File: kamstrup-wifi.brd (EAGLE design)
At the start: 36 x 89.3 mm, 21 parts, among them T1 BT137, T2 BT137, U1 ESP8266-07

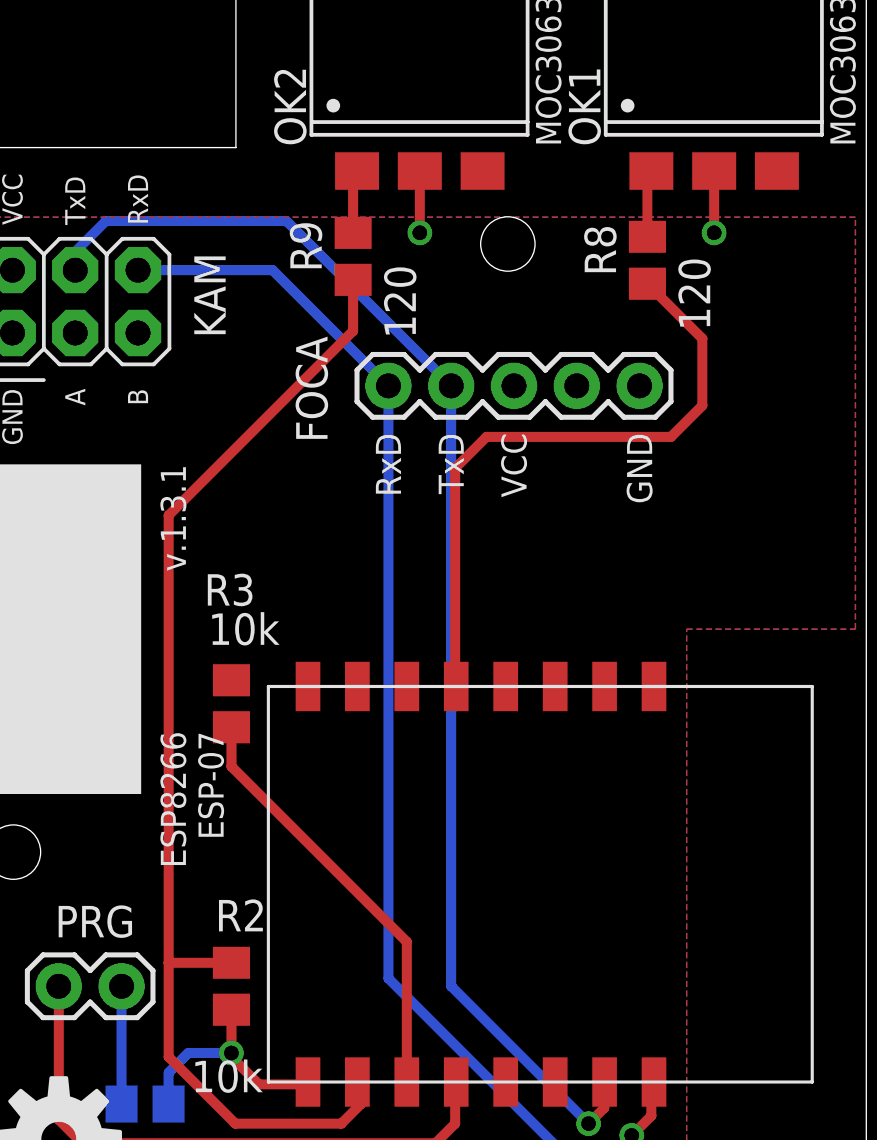
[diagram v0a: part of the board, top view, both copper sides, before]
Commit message: programmer connector moved
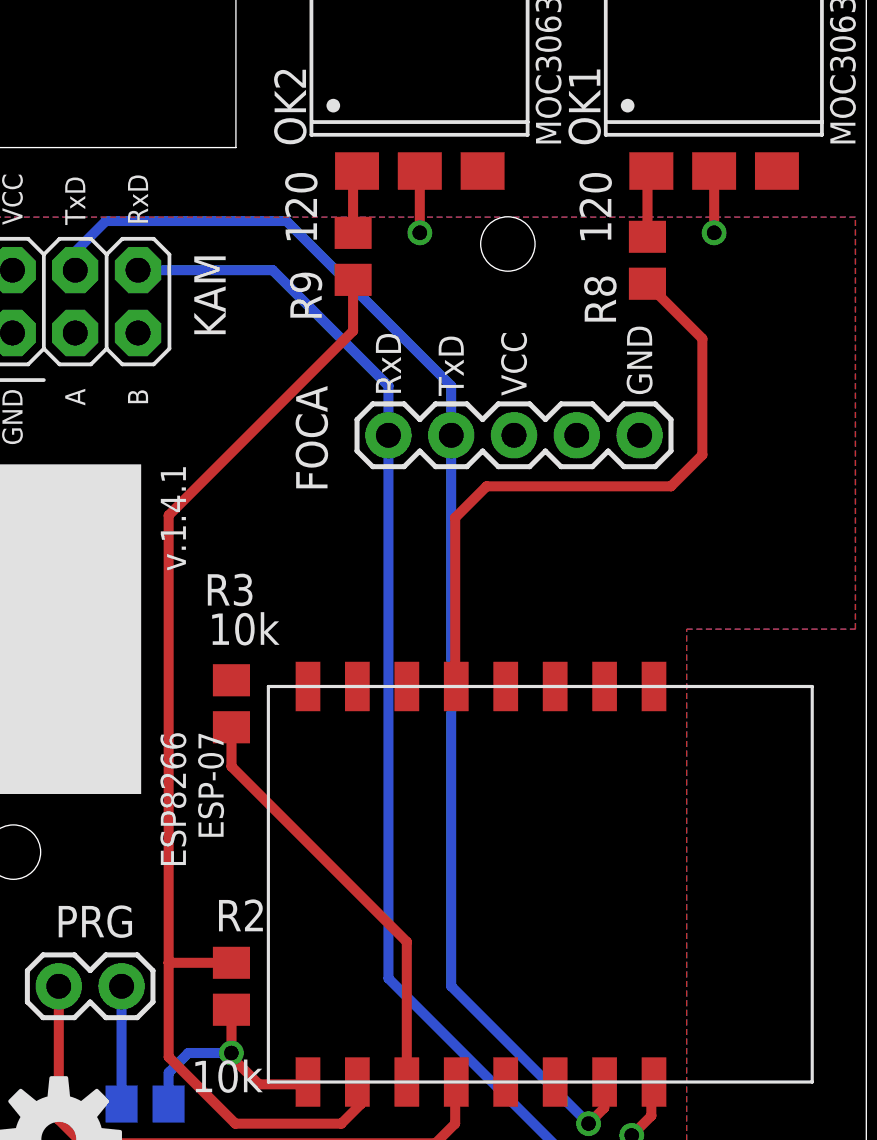
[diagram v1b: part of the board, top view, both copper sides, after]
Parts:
- moved FOCA 2.00 mm to (16.7, 30.9)
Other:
- board text added: "v.1.4.1"
- board text removed: "v.1.3.1"
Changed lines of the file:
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@@
 <?xml version="1.0" encoding="utf-8"?>
 <!DOCTYPE eagle SYSTEM "eagle.dtd">
-<eagle version="8.4.0">
+<eagle version="8.7.1">
 <drawing>
 <settings>
-<setting alwaysvectorfont="yes"/>
+<setting alwaysvectorfont="no"/>
 <setting keepoldvectorfont="yes"/>
 <setting verticaltext="up"/>
@@
 <hole x="1.5" y="14" drill="2.2"/>
 <hole x="21.5" y="38.6" drill="2.2"/>
-<text x="21.74875" y="30.95625" size="1.016" layer="25" rot="R90" align="center-right">VCC</text>
-<text x="19.20875" y="30.95625" size="1.016" layer="25" rot="R90" align="center-right">TxD</text>
-<text x="16.66875" y="30.95625" size="1.016" layer="25" rot="R90" align="center-right">RxD</text>
+<text x="21.74875" y="32.45625" size="1.016" layer="25" rot="R90" align="center-left">VCC</text>
+<text x="19.20875" y="32.45625" size="1.016" layer="25" rot="R90" align="center-left">TxD</text>
+<text x="16.66875" y="32.45625" size="1.016" layer="25" rot="R90" align="center-left">RxD</text>
 <text x="7.46125" y="18.89125" size="1.016" layer="25" ratio="10" rot="R270">ESP8266
 ESP-07</text>
-<text x="7.46125" y="29.68625" size="1.016" layer="25" ratio="15" rot="R270">v.1.3.1</text>
-<text x="26.82875" y="30.95625" size="1.016" layer="25" rot="R90" align="center-right">GND</text>
+<text x="7.46125" y="29.68625" size="1.016" layer="25" ratio="15" rot="R270">v.1.4.1</text>
+<text x="26.82875" y="32.45625" size="1.016" layer="25" rot="R90" align="center-left">GND</text>
 <text x="20.7725" y="75.615" size="1.27" layer="25" ratio="20" rot="R90" align="center">AC IN
 N   L</text>
@@
 <param name="dpMaxLengthDifference" value="10mm"/>
 <param name="dpGapFactor" value="2.5"/>
+<param name="checkAngle" value="0"/>
 <param name="checkFont" value="1"/>
 <param name="checkRestrict" value="1"/>
 <param name="checkStop" value="0"/>
+<param name="checkValues" value="0"/>
 <param name="useDiameter" value="13"/>
 <param name="maxErrors" value="50"/>
@@
 <attribute name="VALUE" x="0.19" y="31.825" size="1.27" layer="27"/>
 </element>
-<element name="FOCA" library="SparkFun-Connectors" package="1X05" value="" x="16.66875" y="32.86125" smashed="yes">
-<attribute name="NAME" x="14.20495" y="30.56255" size="1.27" layer="25" ratio="10" rot="R90"/>
-<attribute name="VALUE" x="15.39875" y="29.68625" size="1.27" layer="27"/>
+<element name="FOCA" library="SparkFun-Connectors" package="1X05" value="" x="16.66875" y="30.86125" smashed="yes">
+<attribute name="NAME" x="14.20495" y="28.56255" size="1.27" layer="25" ratio="10" rot="R90"/>
+<attribute name="VALUE" x="15.39875" y="27.68625" size="1.27" layer="27"/>
 </element>
 <element name="PRG" library="SparkFun-Connectors" package="1X02" value="M02PTH" x="5.87375" y="8.5725" smashed="yes" rot="R180">
@@
 </element>
 <element name="R9" library="rcl" package="R0805" value="120" x="15.24" y="38.1" smashed="yes" rot="R90">
-<attribute name="NAME" x="13.97" y="37.465" size="1.27" layer="25" rot="R90"/>
-<attribute name="VALUE" x="17.78" y="34.76625" size="1.27" layer="25" rot="R90"/>
+<attribute name="NAME" x="13.97" y="35.465" size="1.27" layer="25" rot="R90"/>
+<attribute name="VALUE" x="13.78" y="38.58375" size="1.27" layer="25" rot="R90"/>
 </element>
 <element name="R6" library="rcl" package="R0805" value="330" x="16.8275" y="67.945" smashed="yes" rot="MR180">
@@
 </element>
 <element name="R8" library="rcl" package="R0805" value="120" x="27.14625" y="37.94125" smashed="yes" rot="R90">
-<attribute name="NAME" x="25.87625" y="37.30625" size="1.27" layer="25" rot="R90"/>
-<attribute name="VALUE" x="29.68625" y="35.08375" size="1.27" layer="25" rot="R90"/>
+<attribute name="NAME" x="25.87625" y="35.30625" size="1.27" layer="25" rot="R90"/>
+<attribute name="VALUE" x="25.68625" y="38.58375" size="1.27" layer="25" rot="R90"/>
 </element>
 <element name="R4" library="rcl" package="R0805" value="330" x="27.78125" y="67.945" smashed="yes" rot="MR180">
@@
 <wire x1="25.7175" y1="1.74625" x2="23.8125" y2="1.74625" width="0.4064" layer="16"/>
 <wire x1="23.8125" y1="1.74625" x2="16.66875" y2="8.89" width="0.4064" layer="16"/>
-<wire x1="16.66875" y1="8.89" x2="16.66875" y2="32.86125" width="0.4064" layer="16"/>
+<wire x1="16.66875" y1="8.89" x2="16.66875" y2="30.86125" width="0.4064" layer="16"/>
 <wire x1="6.54" y1="37.54" x2="11.99" y2="37.54" width="0.4064" layer="16"/>
 <wire x1="11.99" y1="37.54" x2="16.66875" y2="32.86125" width="0.4064" layer="16"/>
+<wire x1="16.66875" y1="32.86125" x2="16.66875" y2="30.86125" width="0.4064" layer="16"/>
 </signal>
 <signal name="N$2">
@@
 <wire x1="25.4" y1="4.6875" x2="25.4" y2="3.65125" width="0.4064" layer="1"/>
 <wire x1="25.4" y1="3.65125" x2="24.765" y2="3.01625" width="0.4064" layer="1"/>
-<wire x1="19.20875" y1="32.86125" x2="19.20875" y2="8.5725" width="0.4064" layer="16"/>
+<wire x1="19.20875" y1="30.86125" x2="19.20875" y2="8.5725" width="0.4064" layer="16"/>
 <wire x1="19.20875" y1="8.5725" x2="24.765" y2="3.01625" width="0.4064" layer="16"/>
 <wire x1="5.23875" y1="39.52875" x2="12.54125" y2="39.52875" width="0.4064" layer="16"/>
 <wire x1="12.54125" y1="39.52875" x2="19.20875" y2="32.86125" width="0.4064" layer="16"/>
+<wire x1="19.20875" y1="32.86125" x2="19.20875" y2="30.86125" width="0.4064" layer="16"/>
 </signal>
 <signal name="N$4">
@@
 <wire x1="19.3675" y1="20.745" x2="19.4125" y2="20.7" width="0.4064" layer="1"/>
 <contactref element="R8" pad="1"/>
-<wire x1="19.3675" y1="20.745" x2="19.3675" y2="29.5275" width="0.4064" layer="1"/>
-<wire x1="19.3675" y1="29.5275" x2="20.6375" y2="30.7975" width="0.4064" layer="1"/>
-<wire x1="20.6375" y1="30.7975" x2="28.09875" y2="30.7975" width="0.4064" layer="1"/>
-<wire x1="28.09875" y1="30.7975" x2="29.36875" y2="32.0675" width="0.4064" layer="1"/>
-<wire x1="29.36875" y1="32.0675" x2="29.36875" y2="34.76875" width="0.4064" layer="1"/>
+<wire x1="19.3675" y1="20.745" x2="19.3675" y2="27.5275" width="0.4064" layer="1"/>
+<wire x1="19.3675" y1="27.5275" x2="20.6375" y2="28.7975" width="0.4064" layer="1"/>
+<wire x1="20.6375" y1="28.7975" x2="28.09875" y2="28.7975" width="0.4064" layer="1"/>
+<wire x1="28.09875" y1="28.7975" x2="29.36875" y2="30.0675" width="0.4064" layer="1"/>
+<wire x1="29.36875" y1="30.0675" x2="29.36875" y2="34.76875" width="0.4064" layer="1"/>
 <wire x1="29.36875" y1="34.76875" x2="27.14625" y2="36.99125" width="0.4064" layer="1"/>
 </signal>

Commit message: Sdcard
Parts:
- added U$1: MICROSD_SPI_MODE, con-molex-microsd:MICRO_SD_CONNECTOR
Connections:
- new net N$10: U$1.7, U1.GPIO12
- new net N$17: U$1.3, U1.GPIO13
- new net N$19: U$1.5, U1.GPIO14
- new net N$20: R2.2, U$1.2, U1.GPIO15
- net 3.3V: now also U$1.4
- net GND: now also U$1.6
- net N$11: now also U1.GPIO4; no longer U1.GPIO14
- net N$16: now also U1.GPIO5; no longer R2.2, U1.GPIO15
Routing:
- net N$1: track 51.7 -> 16.6 mm
- net N$2: track 53.3 -> 23.2 mm
- net N$16: track 47.3 -> 44.5 mm
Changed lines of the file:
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@@
 <?xml version="1.0" encoding="utf-8"?>
 <!DOCTYPE eagle SYSTEM "eagle.dtd">
-<eagle version="8.7.1">
+<eagle version="9.0.1">
 <drawing>
 <settings>
@@
 <text x="20.7725" y="75.615" size="1.27" layer="25" ratio="20" rot="R90" align="center">AC IN
 N   L</text>
-<text x="27.6225" y="13.0175" size="1.016" layer="26" font="fixed" rot="MR0">Part            RS#
+<text x="15.4825" y="32.6225" size="1.016" layer="26" font="fixed" rot="MR270">Part            RS#
 JP1, JP2, JP3   821-8701
 KAM             702-2937
@@
 T1, T2          792-0709
 </text>
-<wire x1="28.41625" y1="26.845" x2="14.2875" y2="26.845" width="0.1524" layer="26"/>
-<wire x1="14.2875" y1="26.845" x2="5.08" y2="26.845" width="0.1524" layer="26"/>
-<wire x1="5.08" y1="26.845" x2="5.08" y2="13.81125" width="0.1524" layer="26"/>
-<wire x1="5.08" y1="13.81125" x2="14.2875" y2="13.81125" width="0.1524" layer="26"/>
-<wire x1="14.2875" y1="13.81125" x2="28.41625" y2="13.81125" width="0.1524" layer="26"/>
-<wire x1="28.41625" y1="13.81125" x2="28.41625" y2="26.845" width="0.1524" layer="26"/>
-<wire x1="14.2875" y1="26.845" x2="14.2875" y2="13.81125" width="0.1524" layer="26"/>
+<wire x1="1.655" y1="33.41625" x2="1.655" y2="19.2875" width="0.1524" layer="26"/>
+<wire x1="1.655" y1="19.2875" x2="1.655" y2="10.08" width="0.1524" layer="26"/>
+<wire x1="1.655" y1="10.08" x2="14.68875" y2="10.08" width="0.1524" layer="26"/>
+<wire x1="14.68875" y1="10.08" x2="14.68875" y2="19.2875" width="0.1524" layer="26"/>
+<wire x1="14.68875" y1="19.2875" x2="14.68875" y2="33.41625" width="0.1524" layer="26"/>
+<wire x1="14.68875" y1="33.41625" x2="1.655" y2="33.41625" width="0.1524" layer="26"/>
+<wire x1="1.655" y1="19.2875" x2="14.68875" y2="19.2875" width="0.1524" layer="26"/>
 <wire x1="12.99375" y1="80.06" x2="16.9625" y2="80.06" width="0.254" layer="25"/>
 <wire x1="16.9625" y1="80.06" x2="16.9625" y2="70.2175" width="0.254" layer="25"/>
@@
 <attribute name="VALUE" x="9.36625" y="22.38375" size="1.27" layer="25"/>
 </element>
+<element name="U$1" library="con-molex-microsd" package="MICRO_SD_CONNECTOR" value="MICROSD_SPI_MODE" x="26.5" y="13.5" rot="MR270"/>
 </elements>
 <signals>
@@
 <contactref element="R2" pad="1"/>
 <wire x1="10.31875" y1="7.6225" x2="10.31875" y2="5.87375" width="0.4064" layer="1"/>
+<contactref element="U$1" pad="6"/>
+<wire x1="13.4125" y1="4.7" x2="18.3" y2="10.03" width="0" layer="19" extent="1-16"/>
 </signal>
 <signal name="3.3V">
@@
 <contactref element="U1" pad="VCC"/>
 <contactref element="R3" pad="1"/>
+<contactref element="U$1" pad="4"/>
+<wire x1="13.4125" y1="20.7" x2="18.3" y2="12.23" width="0" layer="19" extent="1-16"/>
 </signal>
 <signal name="N$1">
@@
 <wire x1="27.305" y1="3.33375" x2="27.305" y2="4.5925" width="0.4064" layer="1"/>
 <wire x1="27.305" y1="4.5925" x2="27.4125" y2="4.7" width="0.4064" layer="1"/>
-<wire x1="26.51125" y1="2.54" x2="25.7175" y2="1.74625" width="0.4064" layer="16"/>
-<wire x1="25.7175" y1="1.74625" x2="23.8125" y2="1.74625" width="0.4064" layer="16"/>
-<wire x1="23.8125" y1="1.74625" x2="16.66875" y2="8.89" width="0.4064" layer="16"/>
-<wire x1="16.66875" y1="8.89" x2="16.66875" y2="30.86125" width="0.4064" layer="16"/>
 <wire x1="6.54" y1="37.54" x2="11.99" y2="37.54" width="0.4064" layer="16"/>
 <wire x1="11.99" y1="37.54" x2="16.66875" y2="32.86125" width="0.4064" layer="16"/>
 <wire x1="16.66875" y1="32.86125" x2="16.66875" y2="30.86125" width="0.4064" layer="16"/>
+<wire x1="27.4125" y1="4.7" x2="16.66875" y2="30.86125" width="0" layer="19" extent="1-1"/>
 </signal>
 <signal name="N$2">
@@
 <wire x1="25.4" y1="4.6875" x2="25.4" y2="3.65125" width="0.4064" layer="1"/>
 <wire x1="25.4" y1="3.65125" x2="24.765" y2="3.01625" width="0.4064" layer="1"/>
-<wire x1="19.20875" y1="30.86125" x2="19.20875" y2="8.5725" width="0.4064" layer="16"/>
-<wire x1="19.20875" y1="8.5725" x2="24.765" y2="3.01625" width="0.4064" layer="16"/>
 <wire x1="5.23875" y1="39.52875" x2="12.54125" y2="39.52875" width="0.4064" layer="16"/>
 <wire x1="12.54125" y1="39.52875" x2="19.20875" y2="32.86125" width="0.4064" layer="16"/>
 <wire x1="19.20875" y1="32.86125" x2="19.20875" y2="30.86125" width="0.4064" layer="16"/>
+<wire x1="19.20875" y1="30.86125" x2="25.4125" y2="4.7" width="0" layer="19" extent="1-1"/>
 </signal>
 <signal name="N$4">
@@
 </signal>
 <signal name="N$11">
-<contactref element="U1" pad="GPIO14"/>
-<wire x1="19.3675" y1="20.745" x2="19.4125" y2="20.7" width="0.4064" layer="1"/>
 <contactref element="R8" pad="1"/>
 <wire x1="19.3675" y1="20.745" x2="19.3675" y2="27.5275" width="0.4064" layer="1"/>
@@
 <wire x1="29.36875" y1="30.0675" x2="29.36875" y2="34.76875" width="0.4064" layer="1"/>
 <wire x1="29.36875" y1="34.76875" x2="27.14625" y2="36.99125" width="0.4064" layer="1"/>
+<contactref element="U1" pad="GPIO4"/>
+<wire x1="23.4125" y1="4.7" x2="19.3675" y2="20.745" width="0" layer="19" extent="1-1"/>
 </signal>
 <signal name="N$16">
-<contactref element="U1" pad="GPIO15"/>
-<wire x1="15.39875" y1="4.71375" x2="15.4125" y2="4.7" width="0.4064" layer="1"/>
-<contactref element="R2" pad="2"/>
 <contactref element="R9" pad="1"/>
 <wire x1="15.24" y1="35.08375" x2="15.24" y2="37.15" width="0.4064" layer="1"/>
@@
 <wire x1="14.76375" y1="3.01625" x2="15.5575" y2="3.81" width="0.4064" layer="1"/>
 <wire x1="15.5575" y1="3.81" x2="15.5575" y2="4.555" width="0.4064" layer="1"/>
-<wire x1="15.5575" y1="4.555" x2="15.4125" y2="4.7" width="0.4064" layer="1"/>
-<wire x1="10.31875" y1="9.5225" x2="7.78125" y2="9.5225" width="0.4064" layer="1"/>
 <wire x1="7.78125" y1="9.5225" x2="7.77875" y2="9.525" width="0.4064" layer="1"/>
+<contactref element="U1" pad="GPIO5"/>
+<wire x1="15.5575" y1="4.555" x2="21.4125" y2="4.7" width="0" layer="19" extent="1-1"/>
 </signal>
 <signal name="N$3">
@@
 <wire x1="3.33375" y1="77.62875" x2="3.175" y2="77.47" width="1.016" layer="1"/>
 </signal>
+<signal name="N$10">
+<contactref element="U1" pad="GPIO12"/>
+<contactref element="U$1" pad="7"/>
+<wire x1="18.3" y1="8.93" x2="17.4125" y2="20.7" width="0" layer="19" extent="1-16"/>
+</signal>
+<signal name="N$17">
+<contactref element="U$1" pad="3"/>
+<contactref element="U1" pad="GPIO13"/>
+<wire x1="18.3" y1="13.33" x2="15.4125" y2="20.7" width="0" layer="19" extent="1-16"/>
+</signal>
+<signal name="N$19">
+<contactref element="U1" pad="GPIO14"/>
+<contactref element="U$1" pad="5"/>
+<wire x1="18.3" y1="11.13" x2="19.4125" y2="20.7" width="0" layer="19" extent="1-16"/>
+</signal>
+<signal name="N$20">
+<contactref element="U1" pad="GPIO15"/>
+<contactref element="R2" pad="2"/>
+<wire x1="15.39875" y1="4.71375" x2="15.4125" y2="4.7" width="0.4064" layer="1"/>
+<contactref element="U$1" pad="2"/>
+<wire x1="10.31875" y1="9.5225" x2="18.3" y2="14.43" width="0" layer="19" extent="1-16"/>
+<wire x1="15.39875" y1="4.71375" x2="10.31875" y2="9.5225" width="0" layer="19" extent="1-1"/>
+</signal>
 </signals>
